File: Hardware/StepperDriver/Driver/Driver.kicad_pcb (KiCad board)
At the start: 2 copper layers, 33 parts, among them M1A1 CONN_01X02, M1A2 CONN_01X02, P1 CONN_01X07, Q1 FQP20N06, Q10 2N3704, Q11 FQP20N06, Q12 FQP20N06, Q2 FQP20N06, Q3 2N3704, Q4 2N3704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

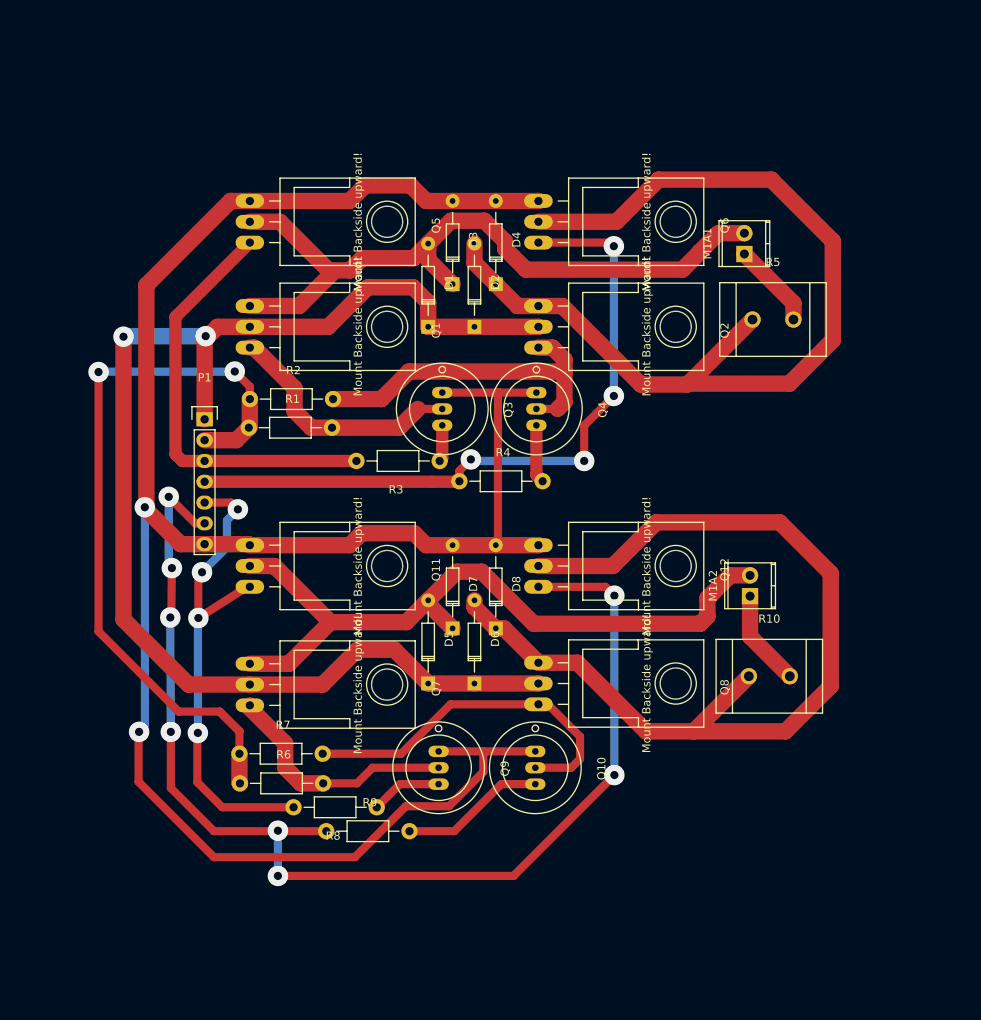
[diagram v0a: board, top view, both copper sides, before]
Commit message: various production tweaks: fixed track layers and footprints
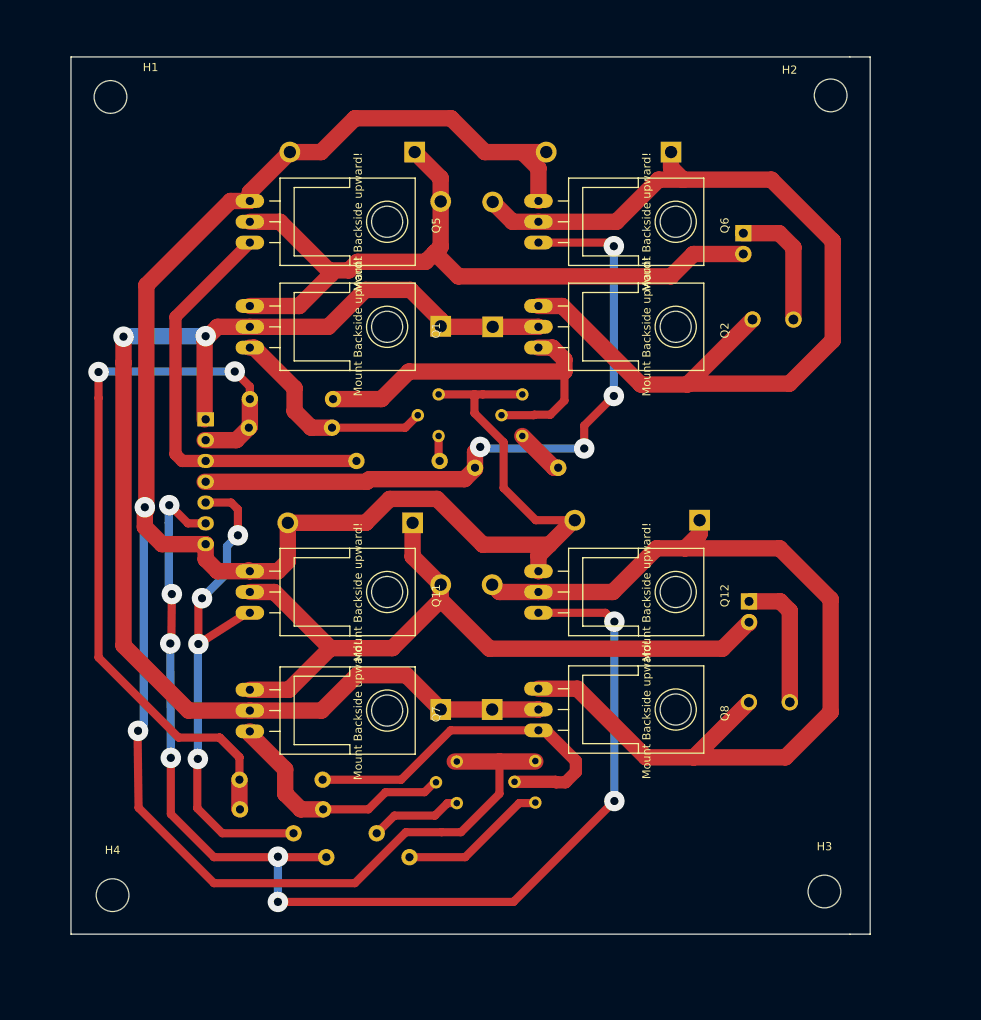
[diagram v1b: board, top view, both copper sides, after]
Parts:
- added H1: CONN_01X01, Mounting_Holes:MountingHole_4mm, F.Cu at (41.5, 42.4)
- added H2: CONN_01X01, Mounting_Holes:MountingHole_4mm, F.Cu at (129.4, 42.2)
- added H3: CONN_01X01, Mounting_Holes:MountingHole_4mm, F.Cu at (128.7, 139.4)
- added H4: CONN_01X01, Mounting_Holes:MountingHole_4mm, F.Cu at (41.7, 139.9)
- D1, D2, D3, D4, D5, D6, D7, D8: footprint Diodes_ThroughHole:Diode_DO-35_SOD27_Horizontal_RM10 -> Diodes_ThroughHole:Diode_DO-201AD_Horizontal_RM15; moved to B.Cu
- M1A1, M1A2, P1, R1, R10, R2, R3, R4, R5, R6, R7, R8, R9: moved to B.Cu
- Q10, Q3, Q4, Q9: footprint Transistors_OldSowjetAera:OldSowjetaera_Transistor_Type-I_BigPads -> TO_SOT_Packages_THT:TO-92_Molded_Wide; moved to B.Cu
- moved D8 28.2 mm to (113.4, 94.1), turned to 180 degrees
- moved D4 26.8 mm to (109.9, 49.1), turned to 180 degrees
- moved D3 16.8 mm to (78.6, 49.1), turned to 180 degrees
- moved D7 13.8 mm to (78.4, 94.4), turned to 180 degrees
- moved D6 3.84 mm to (88.1, 117.2)
- moved D5 3.52 mm to (81.8, 117.2)
- moved Q11 3.18 mm to (58.5, 102.9)
- moved Q12 3.18 mm to (93.7, 102.9)
- moved R6 3.18 mm to (62.4, 129.4)
- moved R8 3.18 mm to (68.9, 132.3)
- moved Q7 3.17 mm to (58.5, 117.3)
- moved Q8 3.17 mm to (93.7, 117.2)
- moved R10 3.17 mm to (121.9, 116.3)
- moved R7 3.17 mm to (62.3, 125.8)
- moved R9 3.17 mm to (72.9, 135.3)
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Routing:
- net GND: track 262.5 -> 303.2 mm
- net Net-(M1A1-Pad1): track 10.5 -> 15.6 mm
- net Net-(M1A2-Pad1): track 11.8 -> 16.6 mm
- net Net-(Q2-Pad1): track 42.4 -> 46.9 mm
- net Net-(D5-Pad2): track 89.5 -> 93.0 mm
- net Net-(D1-Pad2): track 88.5 -> 91.9 mm
- net Net-(Q1-Pad1): track 30.1 -> 26.8 mm
- net /STEPPER1PHASEB1: track 60.2 -> 63.4 mm
- net +9V: track 94.2 -> 97.3 mm
- net Net-(Q9-Pad3): track 8.73 -> 11.1 mm
- net /STEPPER1PHASEB2: track 146.2 -> 148.0 mm
- net Net-(D2-Pad2): track 118.9 -> 117.1 mm
- net +5V: track 159.6 -> 161.2 mm
- net Net-(Q3-Pad3): track 4.48 -> 3.10 mm
- net Net-(Q10-Pad2): track 44.2 -> 45.5 mm
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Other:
- board outline added: 97.6 x 107.1 mm

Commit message: added various pictures of PCB
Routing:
- added copper zone on F.Cu, net GND
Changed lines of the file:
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@@
     (links 62)
     (no_connects 0)
-    (area 36.589499 37.478499 134.289001 144.703001)
+    (area 29.972 32.5755 145.732501 153.098501)
     (thickness 1.6)
     (drawings 6)
@@
   )
   (setup
-    (last_trace_width 1)
+    (last_trace_width 1.5)
     (user_trace_width 1)
     (user_trace_width 1)
@@
     (user_trace_width 3)
     (trace_clearance 0.2)
-    (zone_clearance 0.508)
+    (zone_clearance 0.9)
     (zone_45_only no)
     (trace_min 0.2)
@@
   (segment (start 91.3765 128.651) (end 93.345 128.651) (width 1) (layer F.Cu) (net 21))
   (segment (start 84.7725 135.255) (end 91.3765 128.651) (width 1) (layer F.Cu) (net 21))
+  (zone (net 2) (net_name GND) (layer F.Cu) (hatch edge 0.508)
+    (connect_pads (clearance 0.9))
+    (min_thickness 0.254)
+    (fill yes (arc_segments 16) (thermal_gap 0.508) (thermal_bridge_width 0.508))
+    (polygon
+      (pts
+        (xy 142.24 32.5755) (xy 29.972 32.5755) (xy 30.353 151.4475) (xy 145.7325 153.0985) (xy 142.24 32.5755)
+      )
+    )
+  )
 )
